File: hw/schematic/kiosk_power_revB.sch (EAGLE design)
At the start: 26 parts, among them J1 POWER_JACK, K1 BT-5-S, T1 BC547, T2 BC517, T3 IRLU7843TO251AA

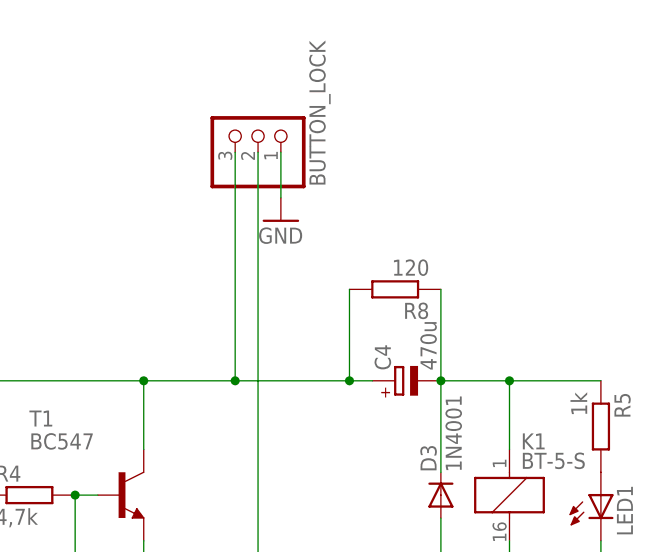
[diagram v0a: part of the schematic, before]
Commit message: hw: schematic: Updated schematic
Increased relay coil series resistance to 220 ohms,
which decreases power consumption.

Signed-off-by: Jan Siegmund <jsiegmun@hm.edu>
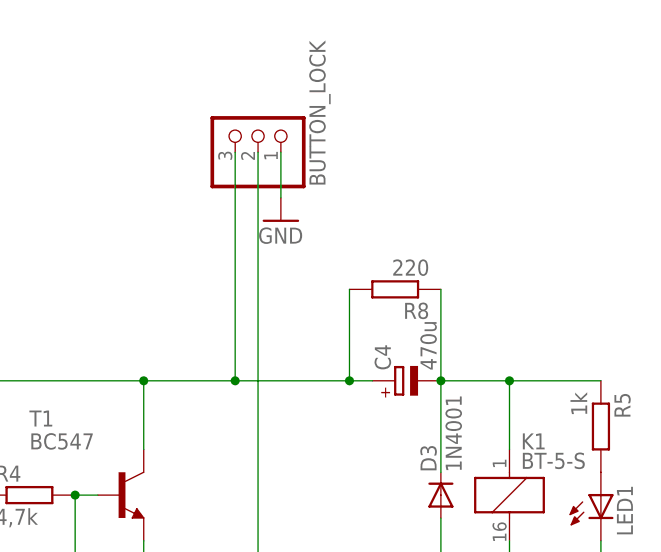
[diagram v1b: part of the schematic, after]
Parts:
- R8: value 120 -> 220
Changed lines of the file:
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@@
 <part name="R7" library="resistor" library_urn="urn:adsk.eagle:library:348" deviceset="R-EU_" device="0207/7" package3d_urn="urn:adsk.eagle:package:25942/1" value="10k"/>
 <part name="C4" library="resistor" library_urn="urn:adsk.eagle:library:348" deviceset="CPOL-EU" device="E2-5" package3d_urn="urn:adsk.eagle:package:25833/1" value="470u"/>
-<part name="R8" library="resistor" library_urn="urn:adsk.eagle:library:348" deviceset="R-EU_" device="0207/7" package3d_urn="urn:adsk.eagle:package:25942/1" value="120"/>
+<part name="R8" library="resistor" library_urn="urn:adsk.eagle:library:348" deviceset="R-EU_" device="0207/7" package3d_urn="urn:adsk.eagle:package:25942/1" value="220"/>
 <part name="GND5" library="supply1" library_urn="urn:adsk.eagle:library:371" deviceset="GND" device=""/>
 <part name="GND6" library="supply1" library_urn="urn:adsk.eagle:library:371" deviceset="GND" device=""/>
